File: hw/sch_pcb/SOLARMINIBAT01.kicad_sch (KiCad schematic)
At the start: 6 parts, among them J7 JUMP_4X2, J8 CONN1_1, J9 CONN1_1

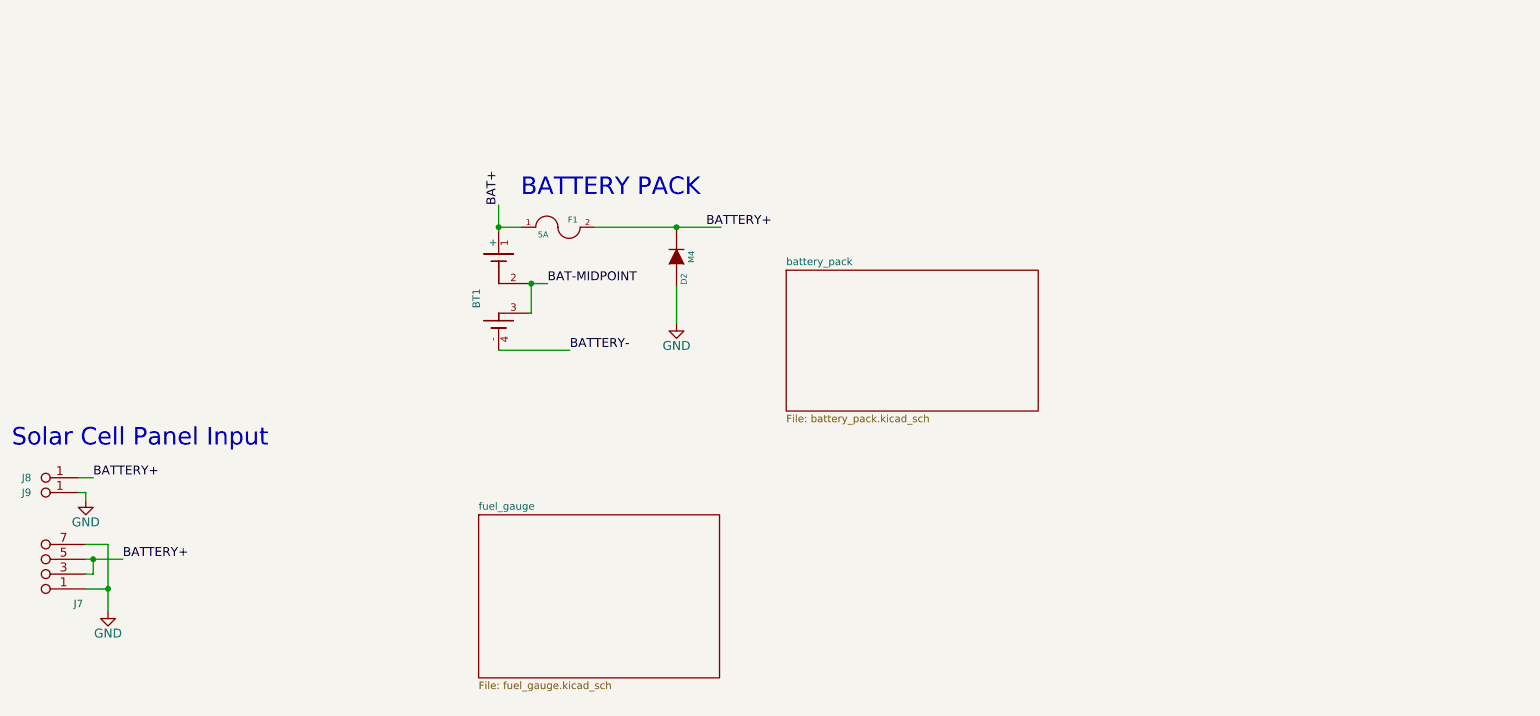
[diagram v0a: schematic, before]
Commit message: Adding input switching regulator.
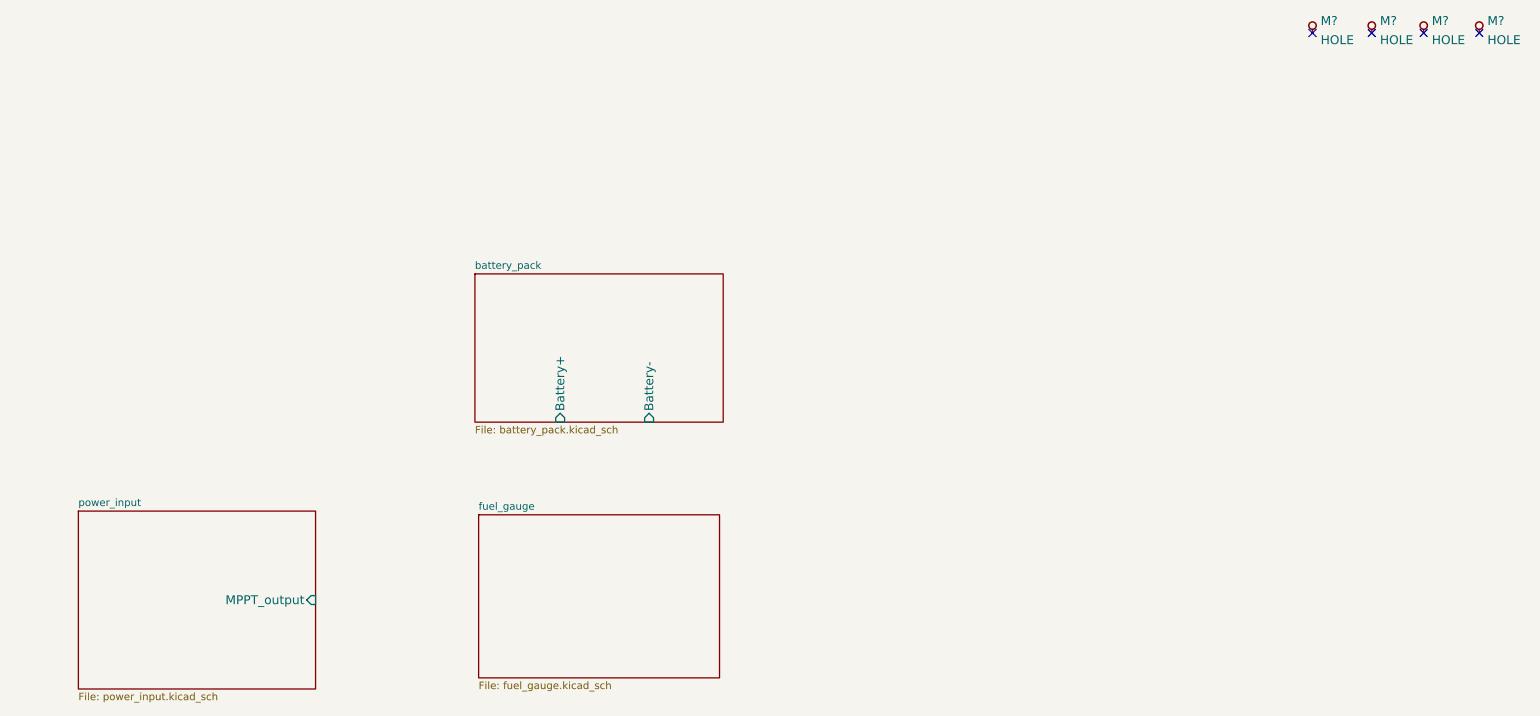
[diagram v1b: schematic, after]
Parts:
- removed BT1: 2x18650_LION-RESCUE-LION2CELL01C, Mlab_Batery:2LION, symbol LION2CELL01D-rescue:2x18650_LION-RESCUE-LION2CELL01C
- removed D2: M4, Mlab_D:SMA_Standard, symbol LION2CELL01D-rescue:DIODE
- removed F1: 5A, Mlab_F:Drzak_2410, symbol LION2CELL01D-rescue:FUSE
- removed J7: JUMP_4X2, Mlab_Pin_Headers:Straight_2x04, symbol LION2CELL01D-rescue:JUMP_4X2
- removed J8, J9: CONN1_1, Mlab_Con:WAGO256, symbol LION2CELL01D-rescue:CONN1_1
- added M? (x4): HOLE, Mlab_Mechanical:MountingHole_3mm, symbol MLAB_MECHANICAL:HOLE
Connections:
- no-connect marks 0 -> 4
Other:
- added sheet power_input (power_input.kicad_sch)
- sheet battery_pack ports: added Battery+, Battery-; removed none
- note removed: "BATTERY PACK"
- note removed: "Solar Cell Panel Input"
